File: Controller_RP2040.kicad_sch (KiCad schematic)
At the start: 11 parts, among them J2 Conn_ARM_SWD_TagConnect_TC203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, U3 NCP1117-3.3

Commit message: BOM update
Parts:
- C4, C5: LCSC (none) -> C2932476; LCSC PN C2932476 -> (none)
- D5: LCSC (none) -> C2976072; LCSC PN C2976072 -> (none)
- D6: LCSC (none) -> C6848499; LCSC PN C6848499 -> (none)
- R13, R14: LCSC (none) -> C138021; LCSC PN C138021 -> (none)
- R3, R4: LCSC (none) -> C105872; LCSC PN C105872 -> (none)
- R5: LCSC (none) -> C106235; LCSC PN C106235 -> (none)
- U3: LCSC (none) -> C233236; LCSC PN C233236 -> (none)
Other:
- moved on the sheet: R13, R14

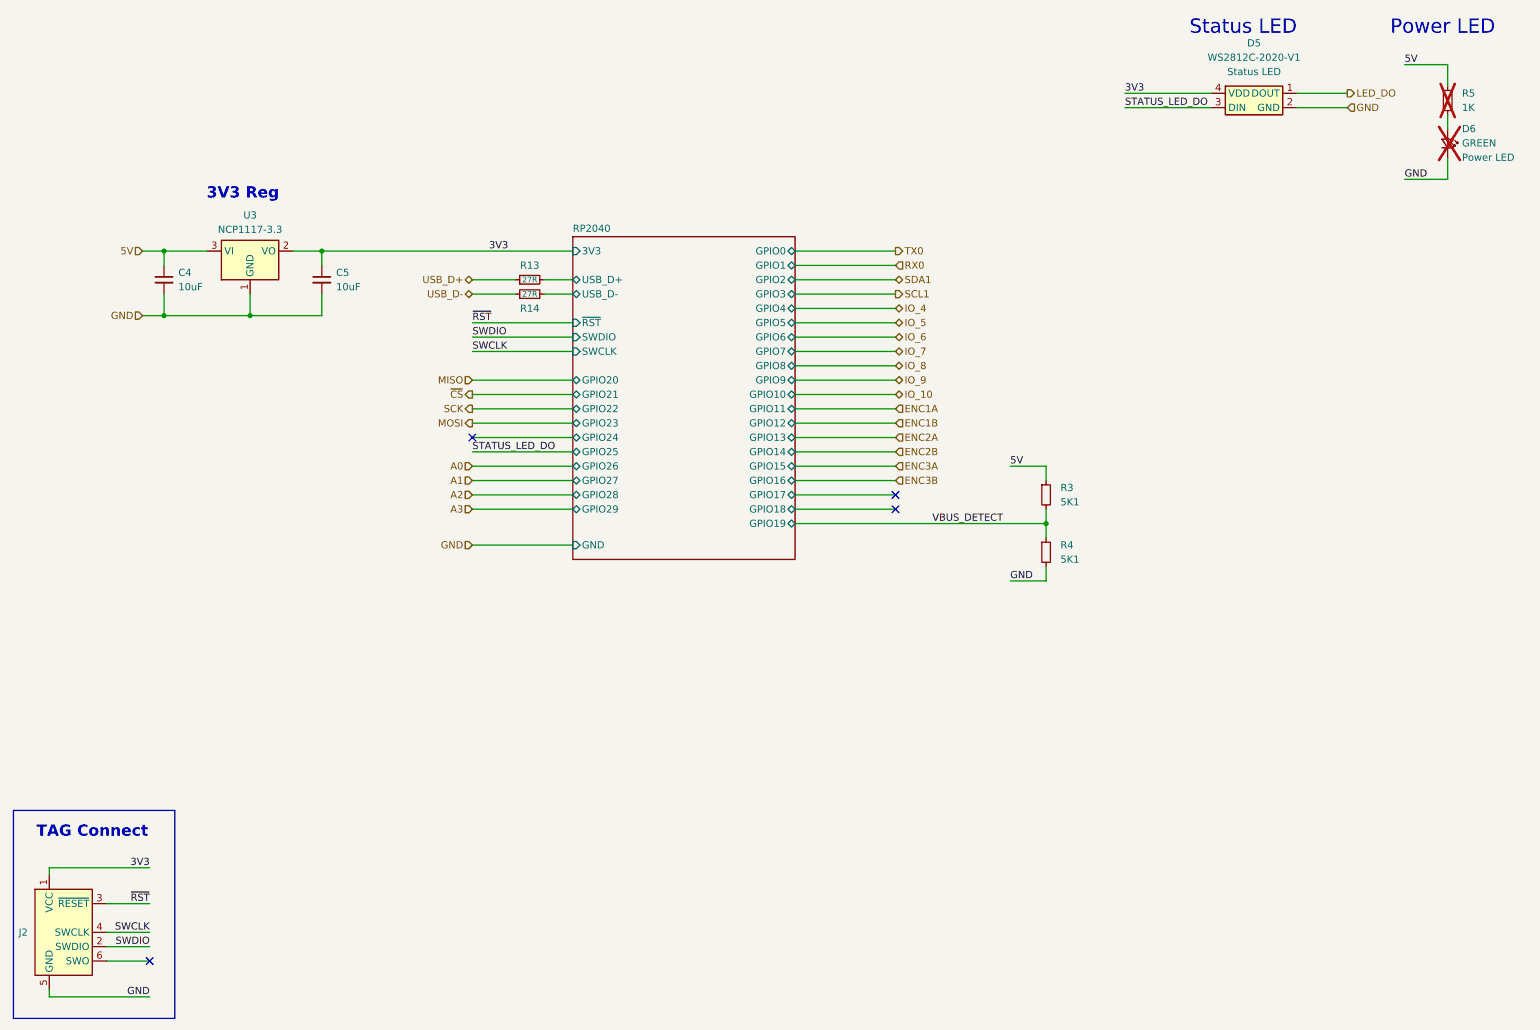
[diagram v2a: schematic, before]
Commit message: Larger 4x4 Anything Keypad (#3)
* Update usb data pins, update to fix 3v3 reg not adj

* Remove Xtal test pad, update PCB

* Update footprint on back light SK6812MINI LED, add more back lights.

* Update PCB back light

* Expand board to 4x5, update rev to b

* Update github workflow

* Rough placement of components. Remove one layer of keys (4x4 -> 4x3)

* More placement, start routing, fix up some schematic connections

* Update tabs

* Update github actions to use main not master for kibot-config checkout

* Review Schematic, Add TRS connector. Continue routing

* Continue routing.

* Finish off routing, clear DRC/ERC's, add missing datasheets

* Update panel size, fix kikit tab link, adjust tab placement and size

* Fix PCB edge

* Update workflow builds

* Rename workflow jobs, use new refactored panelization

* Uses panel file when generating panel datapack

* Update tabs and panel

* Update to 0603 components

Update part of PCB

Finish re-routing 0603

adjust workflow for refactored kibot-config

fill zones to fix FIDs

* Always try to upload artifacts

* refactor documents folder

* add rev_a step models for future reference

Add github actions for images, cad, diff. Rename pcb action

* fetch whole repo for diff

* Remove BOM consolidation comment

* Update github actions

* Add Video action

* test out new action

Update actions

* Update actions

* Update schematic date

* Updates component supplier information

Replaces supplier part numbers with LCSC, Digikey and Mouser numbers
for better component sourcing and availability tracking.

Removes redundant "Supplier PN", "Substitute", and "LCSC PN" properties.
Hides some BOM columns in the project settings.

Also fixes a couple of pin UUIDs and config flags.

* Adds digikey and mouser part numbers to components

Adds digikey and mouser properties to components in the .kicad_pcb file.
Renames "LCSC PN" property to "LCSC" and "Config" property to be more descriptive in certain cases, such as "-LCSC_BOM" or "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
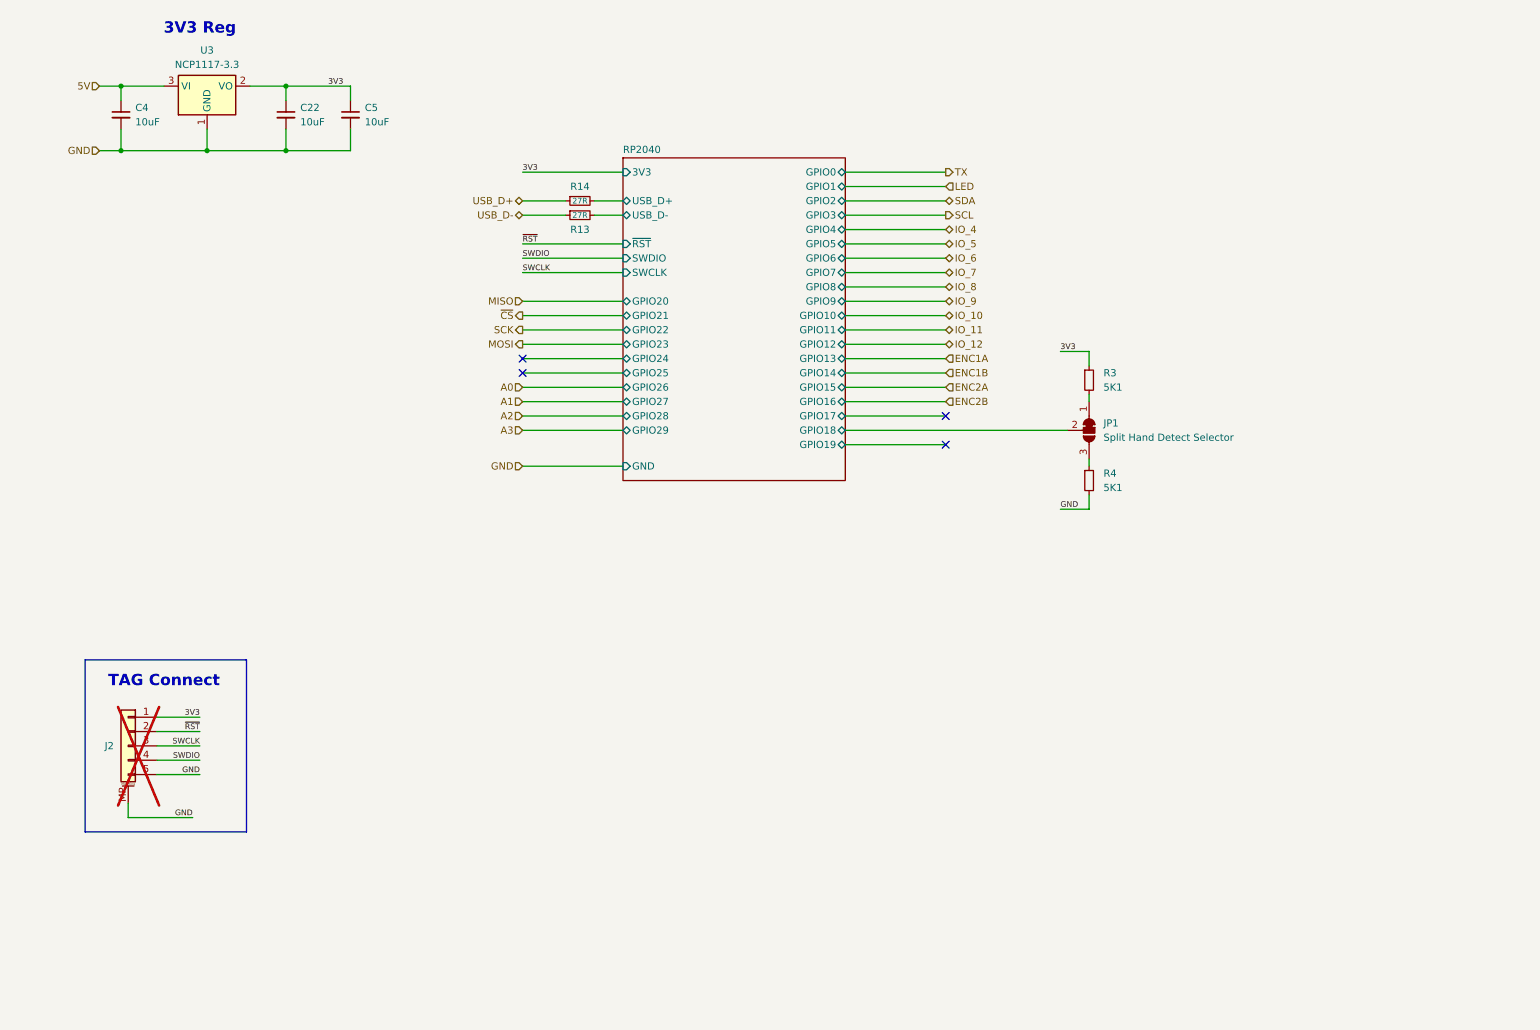
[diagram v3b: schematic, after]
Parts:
- removed D5: WS2812C-2020-V1, Mad_Footprints:WS2812C-2020, symbol Mad_Symbols:WS2812
- removed D6: GREEN, LED_SMD:LED_0603_1608Metric, symbol Device:LED_Small
- removed R5: 1K, Resistor_SMD:R_0402_1005Metric, symbol Device:R_Small
- added C22: 10uF, Capacitor_SMD:C_0805_2012Metric, symbol Device:C_Small
- added JP1: Split Hand Detect Selector, Jumper:SolderJumper-3_P1.3mm_Bridged12_RoundedPad1.0x1.5mm, symbol Jumper:SolderJumper_3_Bridged12
- C4, C5: Supplier PN 311-1869-1-ND -> (none); digikey (none) -> 311-1869-1-ND; mouser (none) -> 603-CC805KKX5R8BB106
- J2: footprint Connector:Tag-Connect_TC2030-IDC-NL_2x03_P1.27mm_Vertical -> Connector_JST:JST_SHL_SM05B-SHLS-TF_1x05-1MP_P1.00mm_Horizontal; symbol Connector:Conn_ARM_SWD_TagConnect_TC2030-NL -> Connector_Generic_MountingPin:Conn_01x05_MountingPin; now not fitted; now in the parts list
- R13, R14: footprint Resistor_SMD:R_0402_1005Metric -> Resistor_SMD:R_0603_1608Metric; MPN RC0402FR-0727RL -> RC0603FR-0727RL; Price $0.16 -> $0.10; Rating RES 27 OHM 1% 1/16W 0402 -> RES 27 OHM 1% 1/16W 0603; Supplier PN YAG3086CT-ND -> (none); digikey (none) -> 311-27.0HRCT-ND; mouser (none) -> 603-RC0603FR-0727RL
- R3, R4: footprint Resistor_SMD:R_0402_1005Metric -> Resistor_SMD:R_0603_1608Metric; MPN RC0402FR-075K1L -> RC0603FR-075K1L; Price $0.16 -> $0.10; Rating RES 5.1K OHM 1% 1/16W 0402 -> RES 5.1K OHM 1% 1/10W 0603; Supplier PN 311-5.10KLRCT-ND -> (none); digikey (none) -> 311-5.10KHRCT-ND; mouser (none) -> 603-RC0603FR-075K1L
- U3: LCSC C233236 -> C146799; MPN NCP1117LPSTADT3G -> NCP1117LPST33T3G; Supplier PN NCP1117LPSTADT3GOSCT-ND -> (none); digikey (none) -> NCP1117LPST33T3GOSCT-ND; mouser (none) -> 863-NCP1117LPST33T3G
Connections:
- net 3V3: now also R3.1, C22.1
- net 5V: no longer R3.1
- net GND: now also J2.MP (MountPin), C22.2
- net RP2040/GPIO18: now also JP1.2 (C)
- net RP2040/USB_D+: now also R14.2; no longer R13.2
- net RP2040/USB_D-: now also R13.2; no longer R14.2
- net SWCLK: now also J2.3 (Pin_3); no longer J2.4 (SWCLK)
- net SWDIO: now also J2.4 (Pin_4); no longer J2.2 (SWDIO)
- net USB_D+: now also R14.1; no longer R13.1
- net USB_D-: now also R13.1; no longer R14.1
- net ~{RST}: now also J2.2 (Pin_2); no longer J2.3 (~{RESET})
- net VBUS_DETECT: no longer names the net of R3.2
- net VBUS_DETECT: now also JP1.1 (A); no longer R4.1
- new net: JP1.3 (B), R4.1
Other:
- note removed: "Power LED"
- note removed: "Status LED"
- moved on the sheet: C4, C5, R13, R14, R3, R4, U3
